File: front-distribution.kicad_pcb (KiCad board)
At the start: 4 copper layers, 103 x 66.8 mm, 91 parts, among them J1 USB_C_Receptacle_USB2.0_14P, J2 Conn_01x23, J3 Conn_01x06, J8 Conn_01x35, J9 Conn_01x08, Q1 AO3400A, Q3 AO3400A, Q4 AO3400A, SW1 SW_Push, U1 TPS7B88, U2 MCP1700x-330xxMB, U3 MAX3232CDR, U4 USBLC6-2SC6, U5 STM32F103C8Tx, U6 SN65HVD1050D, U7 M24C64-R, Y1 8M

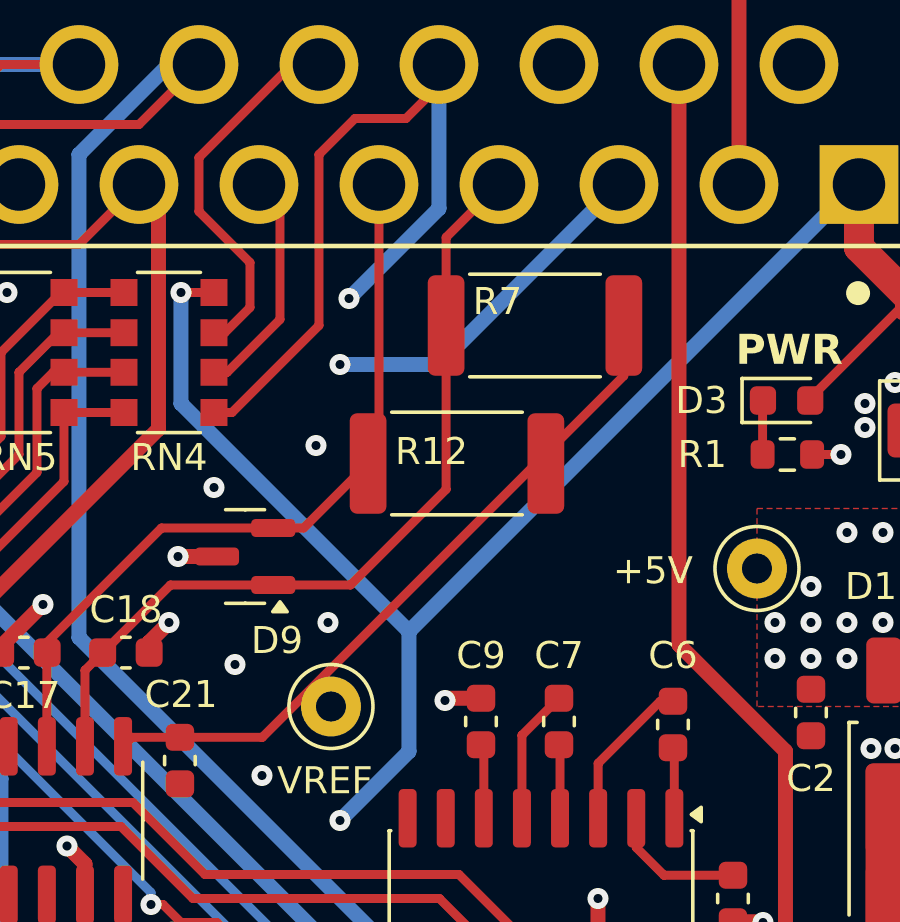
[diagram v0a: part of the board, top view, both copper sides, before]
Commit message: Updated CAN termination resistors
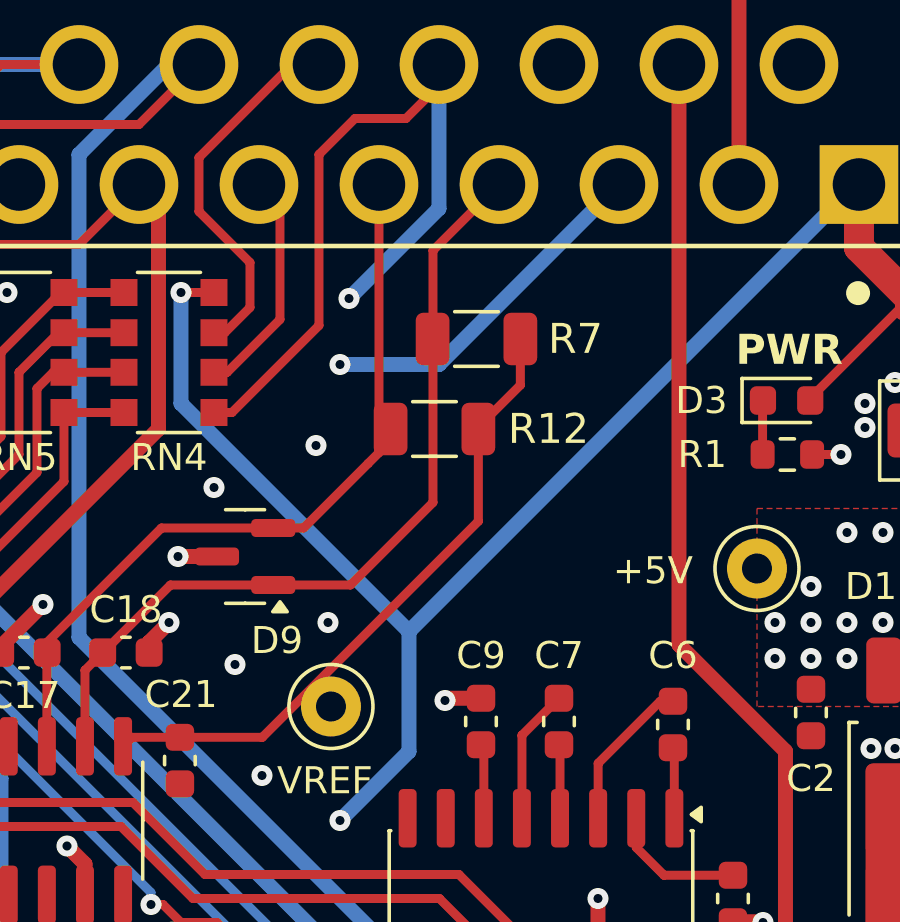
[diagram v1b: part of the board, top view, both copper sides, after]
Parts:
- R12, R7: footprint Resistor_SMD:R_2512_6332Metric -> Resistor_SMD:R_1206_3216Metric
- R16: value 100k -> 10k
- moved R7 2.00 mm to (120.2, 60.1)
- moved R12 1.37 mm to (118.8, 63.1)
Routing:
- net /CAN_VREF: track 23.5 -> 21.6 mm
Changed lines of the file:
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@@
 		)
 	)
-	(footprint "Resistor_SMD:R_2512_6332Metric"
+	(footprint "Resistor_SMD:R_1206_3216Metric"
 		(layer "F.Cu")
-		(at 119.6 64.3 180)
-		(descr "Resistor SMD 2512 (6332 Metric), square (rectangular) end terminal, IPC-7351 nominal, (Body size source: IPC-SM-782 page 72, https://www.pcb-3d.com/wordpress/wp-content/uploads/ipc-sm-782a_amendment_1_and_2.pdf), generated with kicad-footprint-generator")
+		(at 118.85 63.15 180)
+		(descr "Resistor SMD 1206 (3216 Metric), square (rectangular) end terminal, IPC-7351 nominal, (Body size source: IPC-SM-782 page 72, https://www.pcb-3d.com/wordpress/wp-content/uploads/ipc-sm-782a_amendment_1_and_2.pdf), generated with kicad-footprint-generator")
 		(tags "resistor")
 		(property "Reference" "R12"
-			(at 0.85 0.4 180)
+			(at -3.8 0 180)
 			(layer "F.SilkS")
 			(effects
 				(font
-					(size 0.9 0.9)
+					(size 1 1)
 					(thickness 0.15)
 				)
@@
 		)
 		(property "Value" "60R"
-			(at 0 2.63 0)
+			(at 0 1.83 180)
 			(layer "F.Fab")
 			(effects
 				(font
-					(size 0.9 0.9)
+					(size 1 1)
 					(thickness 0.15)
 				)
@@
 		)
 		(property "Datasheet" "~"
-			(at 0 0 0)
+			(at 0 0 180)
 			(layer "F.Fab")
 			(hide yes)
 			(effects
 				(font
-					(size 0.9 0.9)
+					(size 1.27 1.27)
 					(thickness 0.15)
 				)
@@
 		)
 		(property "Description" "Resistor"
-			(at 0 0 0)
+			(at 0 0 180)
 			(layer "F.Fab")
 			(hide yes)
 			(effects
 				(font
-					(size 0.9 0.9)
+					(size 1.27 1.27)
 					(thickness 0.15)
 				)
@@
 		(attr smd)
 		(fp_line
-			(start -2.177064 1.71)
-			(end 2.177064 1.71)
+			(start -0.727064 0.91)
+			(end 0.727064 0.91)
 			(stroke
 				(width 0.12)
@@
 		)
 		(fp_line
-			(start -2.177064 -1.71)
-			(end 2.177064 -1.71)
+			(start -0.727064 -0.91)
+			(end 0.727064 -0.91)
 			(stroke
 				(width 0.12)
@@
 			(layer "F.SilkS")
 		)
-		(fp_poly
-			(pts
-				(xy -3.83 -1.93) (xy 3.83 -1.93) (xy 3.83 1.93) (xy -3.83 1.93)
-			)
+		(fp_rect
+			(start -2.28 -1.13)
+			(end 2.28 1.13)
 			(stroke
 				(width 0.05)
@@
 			(layer "F.CrtYd")
 		)
-		(fp_poly
-			(pts
-				(xy -3.15 -1.6) (xy 3.15 -1.6) (xy 3.15 1.6) (xy -3.15 1.6)
-			)
+		(fp_rect
+			(start -1.6 -0.8)
+			(end 1.6 0.8)
 			(stroke
 				(width 0.1)
@@
 		)
 		(fp_text user "${REFERENCE}"
-			(at 0 0 0)
+			(at 0 0 180)
 			(layer "F.Fab")
 			(effects
 				(font
-					(size 0.9 0.9)
-					(thickness 0.15)
+					(size 0.8 0.8)
+					(thickness 0.12)
 				)
 			)
 		)
 		(pad "1" smd roundrect
-			(at -2.9625 0 180)
-			(size 1.225 3.35)
+			(at -1.4625 0 180)
+			(size 1.125 1.75)
 			(layers "F.Cu" "F.Mask" "F.Paste")
-			(roundrect_rratio 0.204082)
+			(roundrect_rratio 0.222222)
 			(net 18 "/CAN_VREF")
 			(pintype "passive")
 		)
 		(pad "2" smd roundrect
-			(at 2.9625 0 180)
-			(size 1.225 3.35)
+			(at 1.4625 0 180)
+			(size 1.125 1.75)
 			(layers "F.Cu" "F.Mask" "F.Paste")
-			(roundrect_rratio 0.204082)
+			(roundrect_rratio 0.222222)
 			(net 10 "CANH")
 			(pintype "passive")
 		)
 		(embedded_fonts no)
-		(model "${KICAD9_3DMODEL_DIR}/Resistor_SMD.3dshapes/R_2512_6332Metric.step"
+		(model "${KICAD9_3DMODEL_DIR}/Resistor_SMD.3dshapes/R_1206_3216Metric.step"
 			(offset
 				(xyz 0 0 0)
@@
 		(embedded_fonts no)
 	)
-	(footprint "Resistor_SMD:R_2512_6332Metric"
+	(footprint "Resistor_SMD:R_1206_3216Metric"
 		(layer "F.Cu")
-		(at 122.2 59.7 180)
-		(descr "Resistor SMD 2512 (6332 Metric), square (rectangular) end terminal, IPC-7351 nominal, (Body size source: IPC-SM-782 page 72, https://www.pcb-3d.com/wordpress/wp-content/uploads/ipc-sm-782a_amendment_1_and_2.pdf), generated with kicad-footprint-generator")
+		(at 120.25 60.15 180)
+		(descr "Resistor SMD 1206 (3216 Metric), square (rectangular) end terminal, IPC-7351 nominal, (Body size source: IPC-SM-782 page 72, https://www.pcb-3d.com/wordpress/wp-content/uploads/ipc-sm-782a_amendment_1_and_2.pdf), generated with kicad-footprint-generator")
 		(tags "resistor")
 		(property "Reference" "R7"
-			(at 1.25 0.8 180)
+			(at -3.3 0 180)
 			(layer "F.SilkS")
 			(effects
 				(font
-					(size 0.9 0.9)
+					(size 1 1)
 					(thickness 0.15)
 				)
@@
 		)
 		(property "Value" "60R"
-			(at 0 2.63 0)
+			(at 0 1.83 180)
 			(layer "F.Fab")
 			(effects
 				(font
-					(size 0.9 0.9)
+					(size 1 1)
 					(thickness 0.15)
 				)
@@
 		)
 		(property "Datasheet" "~"
-			(at 0 0 0)
+			(at 0 0 180)
 			(layer "F.Fab")
 			(hide yes)
 			(effects
 				(font
-					(size 0.9 0.9)
+					(size 1.27 1.27)
 					(thickness 0.15)
 				)
@@
 		)
 		(property "Description" "Resistor"
-			(at 0 0 0)
+			(at 0 0 180)
 			(layer "F.Fab")
 			(hide yes)
 			(effects
 				(font
-					(size 0.9 0.9)
+					(size 1.27 1.27)
 					(thickness 0.15)
 				)
@@
 		(attr smd)
 		(fp_line
-			(start -2.177064 1.71)
-			(end 2.177064 1.71)
+			(start -0.727064 0.91)
+			(end 0.727064 0.91)
 			(stroke
 				(width 0.12)
@@
 		)
 		(fp_line
-			(start -2.177064 -1.71)
-			(end 2.177064 -1.71)
+			(start -0.727064 -0.91)
+			(end 0.727064 -0.91)
 			(stroke
 				(width 0.12)
@@
 			(layer "F.SilkS")
 		)
-		(fp_poly
-			(pts
-				(xy -3.83 -1.93) (xy 3.83 -1.93) (xy 3.83 1.93) (xy -3.83 1.93)
-			)
+		(fp_rect
+			(start -2.28 -1.13)
+			(end 2.28 1.13)
 			(stroke
 				(width 0.05)
@@
 			(layer "F.CrtYd")
 		)
-		(fp_poly
-			(pts
-				(xy -3.15 -1.6) (xy 3.15 -1.6) (xy 3.15 1.6) (xy -3.15 1.6)
-			)
+		(fp_rect
+			(start -1.6 -0.8)
+			(end 1.6 0.8)
 			(stroke
 				(width 0.1)
@@
 		)
 		(fp_text user "${REFERENCE}"
-			(at 0 0 0)
+			(at 0 0 180)
 			(layer "F.Fab")
 			(effects
 				(font
-					(size 0.9 0.9)
-					(thickness 0.15)
+					(size 0.8 0.8)
+					(thickness 0.12)
 				)
 			)
 		)
 		(pad "1" smd roundrect
-			(at -2.9625 0 180)
-			(size 1.225 3.35)
+			(at -1.4625 0 180)
+			(size 1.125 1.75)
 			(layers "F.Cu" "F.Mask" "F.Paste")
-			(roundrect_rratio 0.204082)
+			(roundrect_rratio 0.222222)
 			(net 18 "/CAN_VREF")
 			(pintype "passive")
 		)
 		(pad "2" smd roundrect
-			(at 2.9625 0 180)
-			(size 1.225 3.35)
+			(at 1.4625 0 180)
+			(size 1.125 1.75)
 			(layers "F.Cu" "F.Mask" "F.Paste")
-			(roundrect_rratio 0.204082)
+			(roundrect_rratio 0.222222)
 			(net 9 "CANL")
 			(pintype "passive")
 		)
 		(embedded_fonts no)
-		(model "${KICAD9_3DMODEL_DIR}/Resistor_SMD.3dshapes/R_2512_6332Metric.step"
+		(model "${KICAD9_3DMODEL_DIR}/Resistor_SMD.3dshapes/R_1206_3216Metric.step"
 			(offset
 				(xyz 0 0 0)
@@
 			)
 		)
-		(property "Value" "100k"
+		(property "Value" "10k"
 			(at 0 1.43 0)
 			(layer "F.Fab")
@@
 	)
 	(segment
-		(start 110.05 68.35)
-		(end 107.797499 70.602501)
+		(start 118.8 65.6)
+		(end 116.05 68.35)
 		(width 0.3)
 		(layer "F.Cu")
@@
 	)
 	(segment
-		(start 119.2375 59.7)
-		(end 119.2375 65.1625)
+		(start 110.05 68.35)
+		(end 107.797499 70.602501)
 		(width 0.3)
 		(layer "F.Cu")
@@
 	)
 	(segment
-		(start 119.2375 65.1625)
-		(end 116.05 68.35)
+		(start 113.475001 68.35)
+		(end 110.05 68.35)
 		(width 0.3)
 		(layer "F.Cu")
@@
 	)
 	(segment
-		(start 113.475001 68.35)
-		(end 110.05 68.35)
+		(start 121 55.000001)
+		(end 118.8 57.200001)
 		(width 0.3)
 		(layer "F.Cu")
@@
 	)
 	(segment
-		(start 119.2375 56.762501)
-		(end 121 55.000001)
+		(start 116.05 68.35)
+		(end 113.475001 68.35)
 		(width 0.3)
 		(layer "F.Cu")
@@
 	)
 	(segment
-		(start 119.2375 59.7)
-		(end 119.2375 56.762501)
+		(start 118.8 57.200001)
+		(end 118.8 65.6)
 		(width 0.3)
 		(layer "F.Cu")
@@
 	)
 	(segment
-		(start 116.05 68.35)
-		(end 113.475001 68.35)
-		(width 0.3)
-		(layer "F.Cu")
-		(net 9)
-	)
-	(segment
 		(start 118.600001 57.4)
 		(end 121 55.000001)
@@
 	)
 	(segment
+		(start 120.3125 63.0875)
+		(end 121.7125 61.6875)
+		(width 0.3)
+		(layer "F.Cu")
+		(net 18)
+	)
+	(segment
+		(start 113.109999 73.427501)
+		(end 120.3125 66.225)
+		(width 0.3)
+		(layer "F.Cu")
+		(net 18)
+	)
+	(segment
 		(start 108.77 73.427501)
 		(end 108.47 73.727501)
@@
 	(segment
 		(start 110.365 73.427501)
-		(end 113.109999 73.427501)
+		(end 108.77 73.427501)
 		(width 0.3)
 		(layer "F.Cu")
@@
 	(segment
 		(start 110.365 73.427501)
-		(end 108.77 73.427501)
+		(end 113.109999 73.427501)
 		(width 0.3)
 		(layer "F.Cu")
@@
 	)
 	(segment
-		(start 113.109999 73.427501)
-		(end 125.1625 61.375)
+		(start 120.3125 66.225)
+		(end 120.3125 63.15)
+		(width 0.3)
+		(layer "F.Cu")
+		(net 18)
+	)
+	(segment
+		(start 120.3125 63.15)
+		(end 120.3125 63.0875)
 		(width 0.3)
 		(layer "F.Cu")
@@
 	)
 	(segment
-		(start 125.1625 61.375)
-		(end 125.1625 59.7)
+		(start 121.7125 61.6875)
+		(end 121.7125 60.15)
 		(width 0.3)
 		(layer "F.Cu")
